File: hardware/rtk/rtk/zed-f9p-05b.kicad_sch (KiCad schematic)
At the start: 8 parts, among them J5 Conn_Coaxial, U4 ZED-F9H-01B

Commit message: PCB: round 1 initial placement complete
Most components in final positions; some will shift during routing.
Schematic tweaks picked up alongside. Add GCT USB4105 datasheet.

Co-Authored-By: Claude Sonnet 4.6 <noreply@anthropic.com>
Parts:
- added C24: 10u, Capacitor_SMD:C_0805_2012Metric_Pad1.18x1.45mm_HandSolder, symbol Device:C_Small
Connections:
- net +3V3: now also C24.2
- net GND: now also C24.1
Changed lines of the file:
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@@
+	)
+	(junction
+		(at 180.34 106.68)
+		(diameter 0)
+		(color 0 0 0 0)
 	)
 	(junction
@@
 	(junction
 		(at 166.37 80.01)
+		(diameter 0)
+		(color 0 0 0 0)
+	)
+	(junction
+		(at 180.34 85.09)
 		(diameter 0)
 		(color 0 0 0 0)
@@
 	(wire
 		(pts
+			(xy 191.77 93.98) (xy 191.77 106.68)
+		)
+		(stroke
+			(width 0)
+			(type default)
+		)
+	)
+	(wire
+		(pts
 			(xy 271.78 72.39) (xy 280.67 72.39)
 		)
@@
 	(wire
 		(pts
+			(xy 180.34 106.68) (xy 191.77 106.68)
+		)
+		(stroke
+			(width 0)
+			(type default)
+		)
+	)
+	(wire
+		(pts
 			(xy 212.09 69.85) (xy 220.98 69.85)
 		)
@@
 	(wire
 		(pts
+			(xy 180.34 85.09) (xy 191.77 85.09)
+		)
+		(stroke
+			(width 0)
+			(type default)
+		)
+	)
+	(wire
+		(pts
 			(xy 212.09 87.63) (xy 212.09 90.17)
 		)
@@
 		(pts
 			(xy 271.78 67.31) (xy 280.67 67.31)
+		)
+		(stroke
+			(width 0)
+			(type default)
+		)
+	)
+	(wire
+		(pts
+			(xy 191.77 85.09) (xy 191.77 88.9)
 		)
 		(stroke
@@
 					(unit 1)
 				)
+			)
+		)
+	)
+	(symbol
+		(lib_id "Device:C_Small")
+		(at 191.77 91.44 180)
+		(unit 1)
+		(body_style 1)
+		(exclude_from_sim no)
+		(in_bom yes)
+		(on_board yes)
+		(in_pos_files yes)
+		(dnp no)
+		(property "Reference" "C24"
+			(at 198.628 91.186 0)
+			(show_name no)
+			(do_not_autoplace no)
+			(effects
+				(font
+					(size 1.27 1.27)
+				)
+				(justify left)
+			)
+		)
+		(property "Value" "10u"
+			(at 198.12 92.964 0)
+			(show_name no)
+			(do_not_autoplace no)
+			(effects
+				(font
+					(size 1.27 1.27)
+				)
+				(justify left)
+			)
+		)
+		(property "Footprint" "Capacitor_SMD:C_0805_2012Metric_Pad1.18x1.45mm_HandSolder"
+			(at 191.77 91.44 0)
+			(hide yes)
+			(show_name no)
+			(do_not_autoplace no)
+			(effects
+				(font
+					(size 1.27 1.27)
+				)
+			)
+		)
+		(property "Datasheet" ""
+			(at 191.77 91.44 0)
+			(hide yes)
+			(show_name no)
+			(do_not_autoplace no)
+			(effects
+				(font
+					(size 1.27 1.27)
+				)
+			)
+		)
+		(property "Description" "Unpolarized capacitor, small symbol"
+			(at 191.77 91.44 0)
+			(hide yes)
+			(show_name no)
+			(do_not_autoplace no)
+			(effects
+				(font
+					(size 1.27 1.27)
+				)
+			)
+		)
+		(pin "1"
+		)
+		(pin "2"
+		)
+		(instances
+			(project "rtk"
+				(path "/608e0f5f-bf55-4b10-9802-aab1430116aa/3c686553-c654-4aca-9ea8-0296b328498f"
+					(reference "C24")
+					(unit 1)
+				)

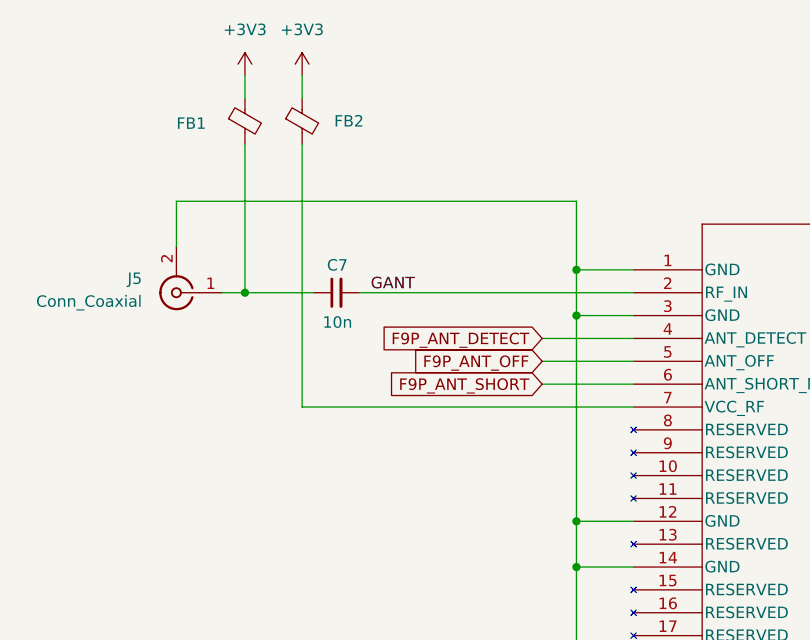
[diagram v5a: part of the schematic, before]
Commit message: BOM: replace FB2 ferrite bead with L2 bias-T inductor (LQW15AN8N0G8ZD)
Ferrite bead was wrong for the GNSS antenna bias-T RF choke — lossy
resistive impedance absorbs signal. Replaced with Murata 8.0nH wire-wound
inductor (0402). Schematic and PCB updated with new symbol/footprint.

Co-Authored-By: Claude Sonnet 4.6 <noreply@anthropic.com>
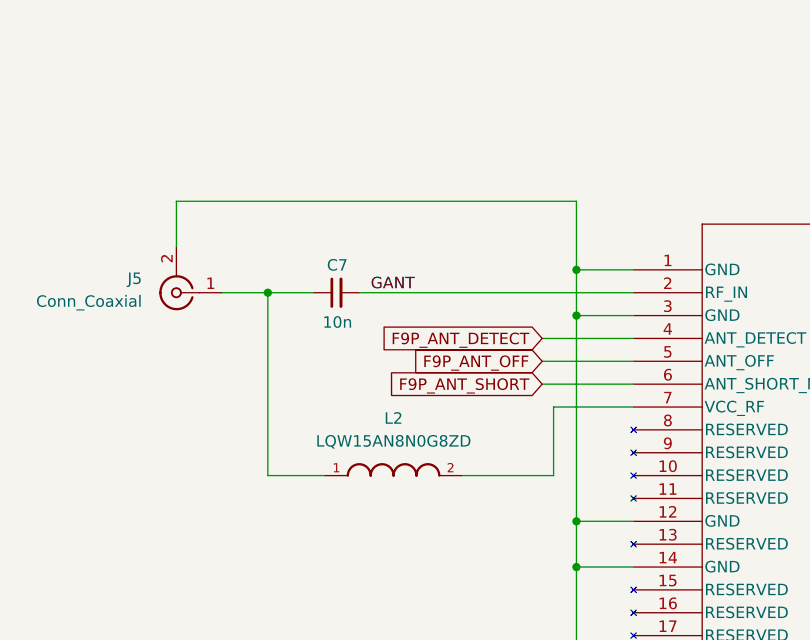
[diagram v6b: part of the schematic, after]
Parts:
- removed FB1, FB2: FerriteBead_Small, Capacitor_SMD:C_0805_2012Metric_Pad1.18x1.45mm_HandSolder, symbol Device:FerriteBead_Small
- added L2: LQW15AN8N0G8ZD, LQW15AN8N0G8ZD:INDC1006X60N, symbol LQW15AN8N0G8ZD:LQW15AN8N0G8ZD
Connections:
- net at C7.1, J5.1 (In): now also L2.1
- net at U4.7 (VCC_RF): now also L2.2

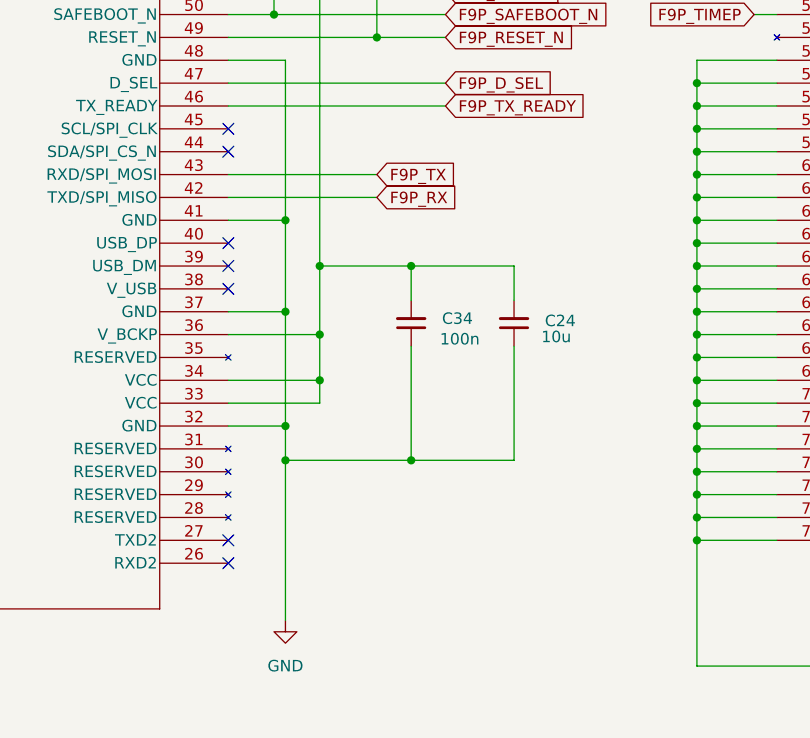
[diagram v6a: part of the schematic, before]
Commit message: Connect F9P UART2 (corrections port) to STM32 UART7
PA8 (UART7_RX) → F9P TXD2, PA15 (UART7_TX) → F9P RXD2.
Dedicated channel for RTCM correction data, keeping UART1 free
for navigation output and UBX configuration.

Co-Authored-By: Claude Sonnet 4.6 <noreply@anthropic.com>
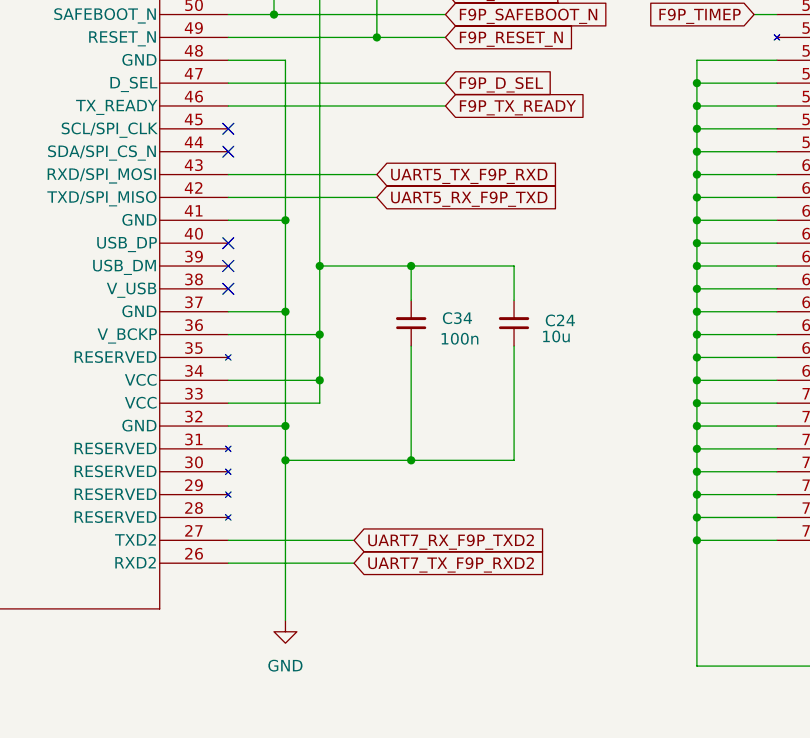
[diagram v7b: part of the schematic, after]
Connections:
- net UART7_TX_F9P_RXD2: now reaches U4.26 (RXD2)
- net UART7_RX_F9P_TXD2: now reaches U4.27 (TXD2)
- net F9P_RX renamed UART5_RX_F9P_TXD
- net F9P_TX renamed UART5_TX_F9P_RXD
- no-connect marks 7 -> 5
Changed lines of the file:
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@@
-	)
-	(no_connect
-		(at 160.02 118.11)
 	)
 	(no_connect
@@
 	)
 	(no_connect
-		(at 160.02 115.57)
-	)
-	(no_connect
 		(at 160.02 85.09)
 	)
@@
 	(wire
 		(pts
+			(xy 160.02 115.57) (xy 173.99 115.57)
+		)
+		(stroke
+			(width 0)
+			(type default)
+		)
+	)
+	(wire
+		(pts
 			(xy 280.67 80.01) (xy 280.67 82.55)
 		)
@@
 		(pts
 			(xy 160.02 59.69) (xy 176.53 59.69)
+		)
+		(stroke
+			(width 0)
+			(type default)
+		)
+	)
+	(wire
+		(pts
+			(xy 160.02 118.11) (xy 173.99 118.11)
 		)
 		(stroke
@@
 		)
 	)
-	(global_label "F9P_RX"
+	(global_label "UART5_RX_F9P_TXD"
 		(shape input)
 		(at 176.53 77.47 0)
@@
 		)
 		(property "Intersheetrefs" "${INTERSHEET_REFS}"
-			(at 186.5304 77.47 0)
+			(at 197.7789 77.47 0)
 			(hide yes)
 			(show_name no)
@@
 		)
 	)
+	(global_label "UART7_RX_F9P_TXD2"
+		(shape input)
+		(at 173.99 115.57 0)
+		(fields_autoplaced yes)
+		(effects
+			(font
+				(size 1.27 1.27)
+			)
+			(justify left)
+		)
+		(property "Intersheetrefs" "${INTERSHEET_REFS}"
+			(at 196.4484 115.57 0)
+			(hide yes)
+			(show_name no)
+			(do_not_autoplace no)
+			(effects
+				(font
+					(size 1.27 1.27)
+				)
+				(justify left)
+			)
+		)
+	)
 	(global_label "F9P_TIMEP"
 		(shape input)
@@
 		)
 	)
+	(global_label "UART7_TX_F9P_RXD2"
+		(shape input)
+		(at 173.99 118.11 0)
+		(fields_autoplaced yes)
+		(effects
+			(font
+				(size 1.27 1.27)
+			)
+			(justify left)
+		)
+		(property "Intersheetrefs" "${INTERSHEET_REFS}"
+			(at 196.4484 118.11 0)
+			(hide yes)
+			(show_name no)
+			(do_not_autoplace no)
+			(effects
+				(font
+					(size 1.27 1.27)
+				)
+				(justify left)
+			)
+		)
+	)
 	(global_label "F9P_RTK_STAT"
 		(shape input)
@@
 		)
 	)
-	(global_label "F9P_TX"
+	(global_label "UART5_TX_F9P_RXD"
 		(shape input)
 		(at 176.53 74.93 0)
@@
 		)
 		(property "Intersheetrefs" "${INTERSHEET_REFS}"
-			(at 186.228 74.93 0)
+			(at 197.7789 74.93 0)
 			(hide yes)
 			(show_name no)
